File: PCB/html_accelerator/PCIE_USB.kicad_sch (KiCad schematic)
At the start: 19 parts, among them U1 MCS9990, U2 AP1513

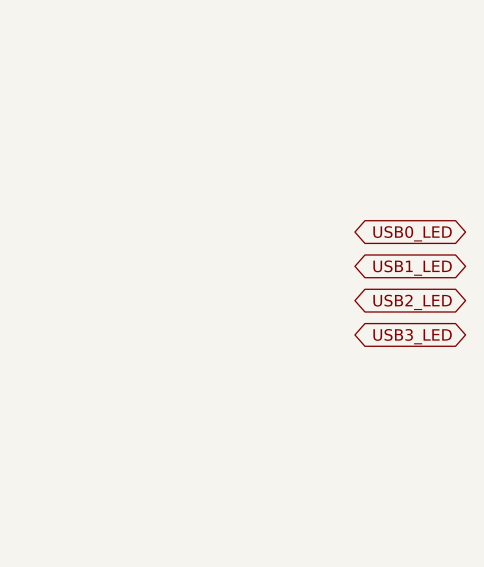
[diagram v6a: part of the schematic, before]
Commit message: provision for LEDs
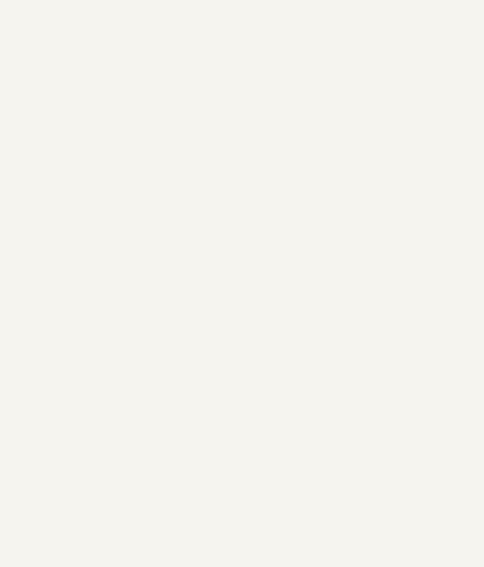
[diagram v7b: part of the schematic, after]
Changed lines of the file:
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@@
-    )
-  )
-  (global_label "USB2_LED" (shape bidirectional) (at 213.36 52.07 180) (fields_autoplaced)
-    (effects (font (size 1.27 1.27)) (justify right))
-    (property "Intersheetrefs" "${INTERSHEET_REFS}" (at 199.9087 52.07 0)
-      (effects (font (size 1.27 1.27)) (justify right))
     )
   )
@@
     )
   )
-  (global_label "USB1_LED" (shape bidirectional) (at 213.36 48.26 180) (fields_autoplaced)
-    (effects (font (size 1.27 1.27)) (justify right))
-    (property "Intersheetrefs" "${INTERSHEET_REFS}" (at 199.9087 48.26 0)
-      (effects (font (size 1.27 1.27)) (justify right))
-    )
-  )
   (global_label "USB2_DP" (shape bidirectional) (at 147.32 78.74 0) (fields_autoplaced)
     (effects (font (size 1.27 1.27)) (justify left))
@@
     )
   )
-  (global_label "USB3_LED" (shape bidirectional) (at 213.36 55.88 180) (fields_autoplaced)
-    (effects (font (size 1.27 1.27)) (justify right))
-    (property "Intersheetrefs" "${INTERSHEET_REFS}" (at 199.9087 55.88 0)
-      (effects (font (size 1.27 1.27)) (justify right))
-    )
-  )
   (global_label "USB1_DP" (shape bidirectional) (at 147.32 63.5 0) (fields_autoplaced)
     (effects (font (size 1.27 1.27)) (justify left))
@@
     )
   )
-  (global_label "USB0_LED" (shape bidirectional) (at 213.36 44.45 180) (fields_autoplaced)
-    (effects (font (size 1.27 1.27)) (justify right))
-    (property "Intersheetrefs" "${INTERSHEET_REFS}" (at 199.9087 44.45 0)
-      (effects (font (size 1.27 1.27)) (justify right))
-    )
-  )
   (symbol (lib_id "power:+12V") (at 44.45 129.54 0) (unit 1)
     (in_bom yes) (on_board yes) (dnp no) (fields_autoplaced)
@@
           (reference "#PWR052") (unit 1)
         )
+        (path "/12b3a7c9-141f-40ba-9ebb-094b58bfa6c7/d3bc6377-21cd-485e-9e5e-2f9ae5072344"
+          (reference "#PWR0112") (unit 1)
+        )
       )
     )
@@
           (reference "R21") (unit 1)
         )
+        (path "/12b3a7c9-141f-40ba-9ebb-094b58bfa6c7/d3bc6377-21cd-485e-9e5e-2f9ae5072344"
+          (reference "R69") (unit 1)
+        )
       )
     )
@@
           (reference "R17") (unit 1)
         )
+        (path "/12b3a7c9-141f-40ba-9ebb-094b58bfa6c7/d3bc6377-21cd-485e-9e5e-2f9ae5072344"
+          (reference "R65") (unit 1)
+        )
       )
     )
@@
           (reference "C33") (unit 1)
         )
+        (path "/12b3a7c9-141f-40ba-9ebb-094b58bfa6c7/d3bc6377-21cd-485e-9e5e-2f9ae5072344"
+          (reference "C67") (unit 1)
+        )
       )
     )
@@
         (path "/12b3a7c9-141f-40ba-9ebb-094b58bfa6c7/665af54b-4239-4192-942b-b320317cb76f"
           (reference "R18") (unit 1)
+        )
+        (path "/12b3a7c9-141f-40ba-9ebb-094b58bfa6c7/d3bc6377-21cd-485e-9e5e-2f9ae5072344"
+          (reference "R66") (unit 1)
         )
       )
@@
         (path "/12b3a7c9-141f-40ba-9ebb-094b58bfa6c7/665af54b-4239-4192-942b-b320317cb76f"
           (reference "#PWR056") (unit 1)
+        )
+        (path "/12b3a7c9-141f-40ba-9ebb-094b58bfa6c7/d3bc6377-21cd-485e-9e5e-2f9ae5072344"
+          (reference "#PWR0116") (unit 1)
         )
       )
@@
           (reference "U2") (unit 1)
         )
+        (path "/12b3a7c9-141f-40ba-9ebb-094b58bfa6c7/d3bc6377-21cd-485e-9e5e-2f9ae5072344"
+          (reference "U13") (unit 1)
+        )
       )
     )
@@
         (path "/12b3a7c9-141f-40ba-9ebb-094b58bfa6c7/665af54b-4239-4192-942b-b320317cb76f"
           (reference "#PWR050") (unit 1)
+        )
+        (path "/12b3a7c9-141f-40ba-9ebb-094b58bfa6c7/d3bc6377-21cd-485e-9e5e-2f9ae5072344"
+          (reference "#PWR0110") (unit 1)
         )
       )
@@
           (reference "#PWR057") (unit 1)
         )
+        (path "/12b3a7c9-141f-40ba-9ebb-094b58bfa6c7/d3bc6377-21cd-485e-9e5e-2f9ae5072344"
+          (reference "#PWR0117") (unit 1)
+        )
       )
     )
@@
         (path "/12b3a7c9-141f-40ba-9ebb-094b58bfa6c7/665af54b-4239-4192-942b-b320317cb76f"
           (reference "#PWR055") (unit 1)
+        )
+        (path "/12b3a7c9-141f-40ba-9ebb-094b58bfa6c7/d3bc6377-21cd-485e-9e5e-2f9ae5072344"
+          (reference "#PWR0115") (unit 1)
         )
       )
@@
           (reference "U1") (unit 4)
         )
+        (path "/12b3a7c9-141f-40ba-9ebb-094b58bfa6c7/d3bc6377-21cd-485e-9e5e-2f9ae5072344"
+          (reference "U12") (unit 4)
+        )
       )
     )
@@
           (reference "L1") (unit 1)
         )
+        (path "/12b3a7c9-141f-40ba-9ebb-094b58bfa6c7/d3bc6377-21cd-485e-9e5e-2f9ae5072344"
+          (reference "L2") (unit 1)
+        )
       )
     )
@@
           (reference "R13") (unit 1)
         )
+        (path "/12b3a7c9-141f-40ba-9ebb-094b58bfa6c7/d3bc6377-21cd-485e-9e5e-2f9ae5072344"
+          (reference "R61") (unit 1)
+        )
       )
     )
@@
           (reference "C34") (unit 1)
         )
+        (path "/12b3a7c9-141f-40ba-9ebb-094b58bfa6c7/d3bc6377-21cd-485e-9e5e-2f9ae5072344"
+          (reference "C68") (unit 1)
+        )
       )
     )
@@
         (path "/12b3a7c9-141f-40ba-9ebb-094b58bfa6c7/665af54b-4239-4192-942b-b320317cb76f"
           (reference "R12") (unit 1)
+        )
+        (path "/12b3a7c9-141f-40ba-9ebb-094b58bfa6c7/d3bc6377-21cd-485e-9e5e-2f9ae5072344"
+          (reference "R60") (unit 1)
         )
       )
@@
           (reference "#PWR051") (unit 1)
         )
+        (path "/12b3a7c9-141f-40ba-9ebb-094b58bfa6c7/d3bc6377-21cd-485e-9e5e-2f9ae5072344"
+          (reference "#PWR0111") (unit 1)
+        )
       )
     )
@@
           (reference "D1") (unit 1)
         )
+        (path "/12b3a7c9-141f-40ba-9ebb-094b58bfa6c7/d3bc6377-21cd-485e-9e5e-2f9ae5072344"
+          (reference "D2") (unit 1)
+        )
       )
     )
@@
           (reference "R14") (unit 1)
         )
+        (path "/12b3a7c9-141f-40ba-9ebb-094b58bfa6c7/d3bc6377-21cd-485e-9e5e-2f9ae5072344"
+          (reference "R62") (unit 1)
+        )
       )
     )
@@
         (path "/12b3a7c9-141f-40ba-9ebb-094b58bfa6c7/665af54b-4239-4192-942b-b320317cb76f"
           (reference "R19") (unit 1)
+        )
+        (path "/12b3a7c9-141f-40ba-9ebb-094b58bfa6c7/d3bc6377-21cd-485e-9e5e-2f9ae5072344"
+          (reference "R67") (unit 1)
         )
       )
@@
           (reference "#PWR054") (unit 1)
         )
+        (path "/12b3a7c9-141f-40ba-9ebb-094b58bfa6c7/d3bc6377-21cd-485e-9e5e-2f9ae5072344"
+          (reference "#PWR0114") (unit 1)
+        )
       )
     )
@@
           (reference "R16") (unit 1)
         )
+        (path "/12b3a7c9-141f-40ba-9ebb-094b58bfa6c7/d3bc6377-21cd-485e-9e5e-2f9ae5072344"
+          (reference "R64") (unit 1)
+        )
       )
     )
@@
           (reference "R20") (unit 1)
         )
+        (path "/12b3a7c9-141f-40ba-9ebb-094b58bfa6c7/d3bc6377-21cd-485e-9e5e-2f9ae5072344"
+          (reference "R68") (unit 1)
+        )
       )
     )
@@
           (reference "#PWR053") (unit 1)
         )
+        (path "/12b3a7c9-141f-40ba-9ebb-094b58bfa6c7/d3bc6377-21cd-485e-9e5e-2f9ae5072344"
+          (reference "#PWR0113") (unit 1)
+        )
       )
     )
@@
           (reference "R15") (unit 1)
         )
+        (path "/12b3a7c9-141f-40ba-9ebb-094b58bfa6c7/d3bc6377-21cd-485e-9e5e-2f9ae5072344"
+          (reference "R63") (unit 1)
+        )
       )
     )
@@
           (reference "R10") (unit 1)
         )
+        (path "/12b3a7c9-141f-40ba-9ebb-094b58bfa6c7/d3bc6377-21cd-485e-9e5e-2f9ae5072344"
+          (reference "R58") (unit 1)
+        )
       )
     )
@@
           (reference "R11") (unit 1)
         )
+        (path "/12b3a7c9-141f-40ba-9ebb-094b58bfa6c7/d3bc6377-21cd-485e-9e5e-2f9ae5072344"
+          (reference "R59") (unit 1)
+        )
       )
     )
@@
           (reference "C32") (unit 1)
         )
-      )
+        (path "/12b3a7c9-141f-40ba-9ebb-094b58bfa6c7/d3bc6377-21cd-485e-9e5e-2f9ae5072344"
+          (reference "C66") (unit 1)
+        )
+      )

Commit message: 3d part models, PCB netlist imported
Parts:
- C28, C33: footprint (none) -> Capacitor_SMD:C_0805_2012Metric_Pad1.18x1.45mm_HandSolder
- R20: footprint (none) -> Resistor_SMD:R_0805_2012Metric_Pad1.20x1.40mm_HandSolder
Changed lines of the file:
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@@
       (effects (font (size 1.27 1.27)))
     )
-    (property "Footprint" "" (at 138.176 165.354 90)
+    (property "Footprint" "Resistor_SMD:R_0805_2012Metric_Pad1.20x1.40mm_HandSolder" (at 138.176 165.354 90)
       (effects (font (size 1.27 1.27)) hide)
     )
@@
       (effects (font (size 1.27 1.27)))
     )
-    (property "Footprint" "" (at 79.756 100.584 90)
+    (property "Footprint" "Resistor_SMD:R_0805_2012Metric_Pad1.20x1.40mm_HandSolder" (at 79.756 100.584 90)
       (effects (font (size 1.27 1.27)) hide)
     )
@@
       (effects (font (size 1.27 1.27)) (justify left))
     )
-    (property "Footprint" "" (at 44.45 154.94 0)
+    (property "Footprint" "Capacitor_SMD:C_0805_2012Metric_Pad1.18x1.45mm_HandSolder" (at 44.45 154.94 0)
       (effects (font (size 1.27 1.27)) hide)
     )
@@
       (effects (font (size 1.27 1.27)))
     )
-    (property "Footprint" "" (at 57.404 150.114 90)
+    (property "Footprint" "Resistor_SMD:R_0805_2012Metric_Pad1.20x1.40mm_HandSolder" (at 57.404 150.114 90)
       (effects (font (size 1.27 1.27)) hide)
     )
@@
       (effects (font (size 1.27 1.27)))
     )
-    (property "Footprint" "" (at 81.026 35.814 90)
+    (property "Footprint" "Resistor_SMD:R_0805_2012Metric_Pad1.20x1.40mm_HandSolder" (at 81.026 35.814 90)
       (effects (font (size 1.27 1.27)) hide)
     )
@@
       (effects (font (size 1.27 1.27)) (justify left))
     )
-    (property "Footprint" "" (at 148.59 154.94 0)
+    (property "Footprint" "Capacitor_SMD:C_0805_2012Metric_Pad1.18x1.45mm_HandSolder" (at 148.59 154.94 0)
       (effects (font (size 1.27 1.27)) hide)
     )
@@
       (effects (font (size 1.27 1.27)))
     )
-    (property "Footprint" "" (at 73.406 35.814 90)
+    (property "Footprint" "Resistor_SMD:R_0805_2012Metric_Pad1.20x1.40mm_HandSolder" (at 73.406 35.814 90)
       (effects (font (size 1.27 1.27)) hide)
     )
@@
       (effects (font (size 1.27 1.27)))
     )
-    (property "Footprint" "" (at 55.626 100.584 90)
+    (property "Footprint" "Resistor_SMD:R_0805_2012Metric_Pad1.20x1.40mm_HandSolder" (at 55.626 100.584 90)
       (effects (font (size 1.27 1.27)) hide)
     )
@@
       (effects (font (size 1.27 1.27)))
     )
-    (property "Footprint" "" (at 138.176 151.384 90)
+    (property "Footprint" "Resistor_SMD:R_0805_2012Metric_Pad1.20x1.40mm_HandSolder" (at 138.176 151.384 90)
       (effects (font (size 1.27 1.27)) hide)
     )
@@
       (effects (font (size 1.27 1.27)))
     )
-    (property "Footprint" "" (at 72.136 100.584 90)
+    (property "Footprint" "Resistor_SMD:R_0805_2012Metric_Pad1.20x1.40mm_HandSolder" (at 72.136 100.584 90)
       (effects (font (size 1.27 1.27)) hide)
     )
@@
       (effects (font (size 1.27 1.27)))
     )
-    (property "Footprint" "" (at 51.816 164.084 90)
+    (property "Footprint" "Resistor_SMD:R_0805_2012Metric_Pad1.20x1.40mm_HandSolder" (at 51.816 164.084 90)
       (effects (font (size 1.27 1.27)) hide)
     )
@@
       (effects (font (size 1.27 1.27)))
     )
-    (property "Footprint" "" (at 64.516 100.584 90)
+    (property "Footprint" "Resistor_SMD:R_0805_2012Metric_Pad1.20x1.40mm_HandSolder" (at 64.516 100.584 90)
       (effects (font (size 1.27 1.27)) hide)
     )
@@
       (effects (font (size 1.27 1.27)))
     )
-    (property "Footprint" "" (at 56.896 35.814 90)
+    (property "Footprint" "Resistor_SMD:R_0805_2012Metric_Pad1.20x1.40mm_HandSolder" (at 56.896 35.814 90)
       (effects (font (size 1.27 1.27)) hide)
     )
@@
       (effects (font (size 1.27 1.27)))
     )
-    (property "Footprint" "" (at 65.786 35.814 90)
+    (property "Footprint" "Resistor_SMD:R_0805_2012Metric_Pad1.20x1.40mm_HandSolder" (at 65.786 35.814 90)
       (effects (font (size 1.27 1.27)) hide)
     )
@@
       (effects (font (size 1.27 1.27)) (justify left))
     )
-    (property "Footprint" "" (at 64.4652 153.67 0)
-      (effects (font (size 1.27 1.27)) hide)
-    )
+    (property "Footprint" "Capacitor_SMD:C_0805_2012Metric_Pad1.18x1.45mm_HandSolder" (at 64.4652 153.67 0)
+      (effects (font (size 1.27 1.27)) hide)
+    )
